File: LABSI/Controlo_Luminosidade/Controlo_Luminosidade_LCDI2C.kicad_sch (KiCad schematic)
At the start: 43 parts, among them J1 Barrel_Jack_Switch, J10 Conn_01x03_Socket, J2 Barrel_Jack_Switch, J3 Conn_01x05_Pin, J4 Conn_01x04_Pin, J5 Conn_01x04_Pin, J6 AVR-ISP-6, J7 Conn_01x03_Pin, J8 Conn_01x03_Pin, J9 Conn_01x05_Pin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

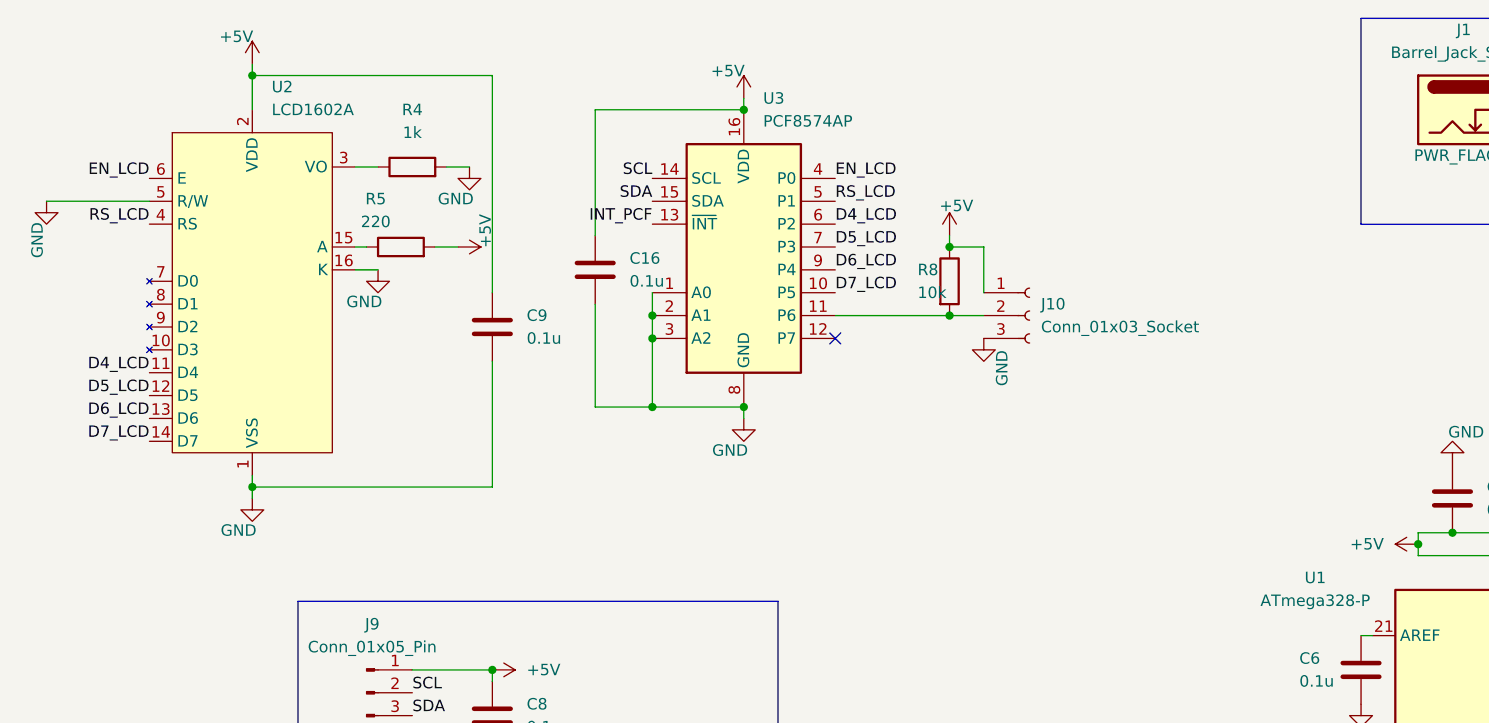
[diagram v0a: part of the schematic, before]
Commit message: added lcd through i2c, code for timer1(servo)
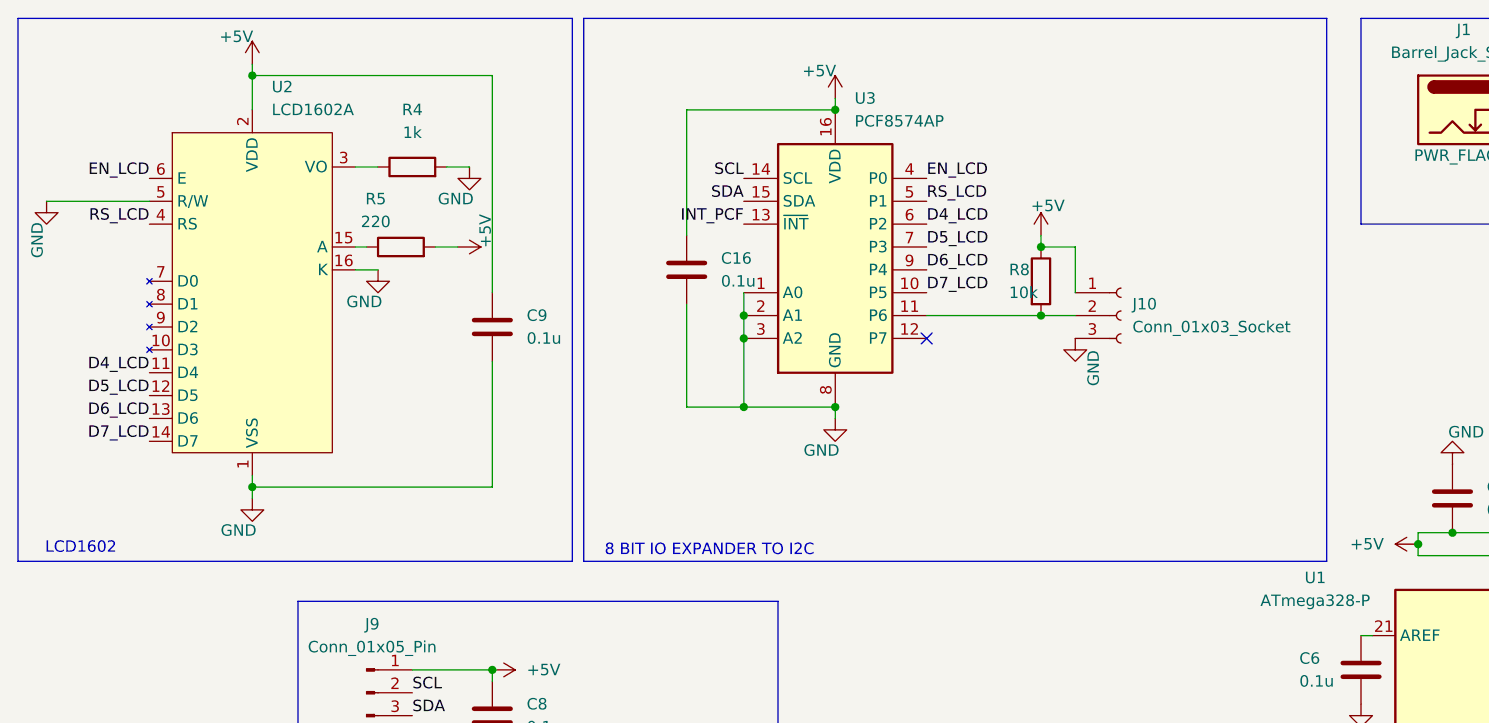
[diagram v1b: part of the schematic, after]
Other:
- note added: "8 BIT IO EXPANDER TO I2C"
- note added: "LCD1602"
- moved on the sheet: C16, J10, R8, U3
